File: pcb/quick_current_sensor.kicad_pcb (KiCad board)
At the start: 2 copper layers, 66.2 x 51.8 mm, 23 parts, among them J1 +Vcc, J2 GND, J3 +LOAD, J4 -LOAD, J5 Vout, J6 GND, Q1 MTP2P50E, U1 LM358N, U2 TL431LP

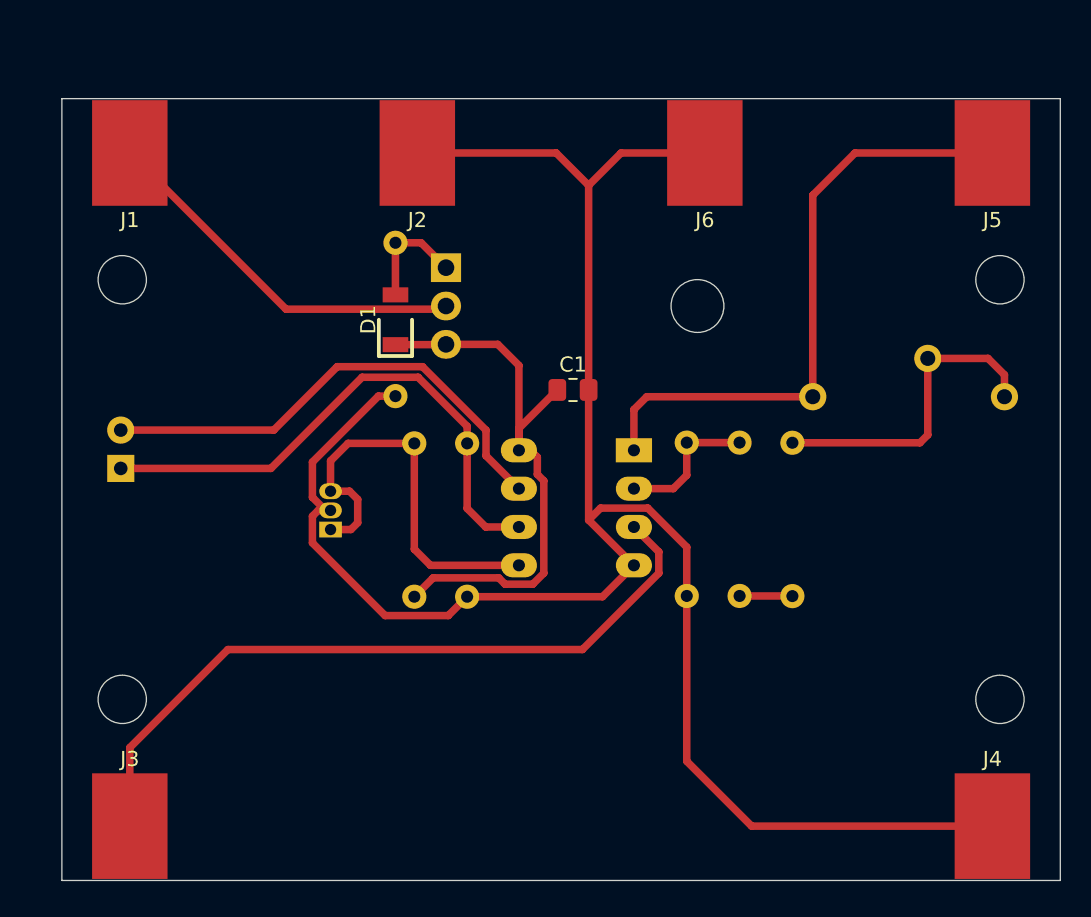
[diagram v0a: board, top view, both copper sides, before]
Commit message: add Rs footprint and 3d model
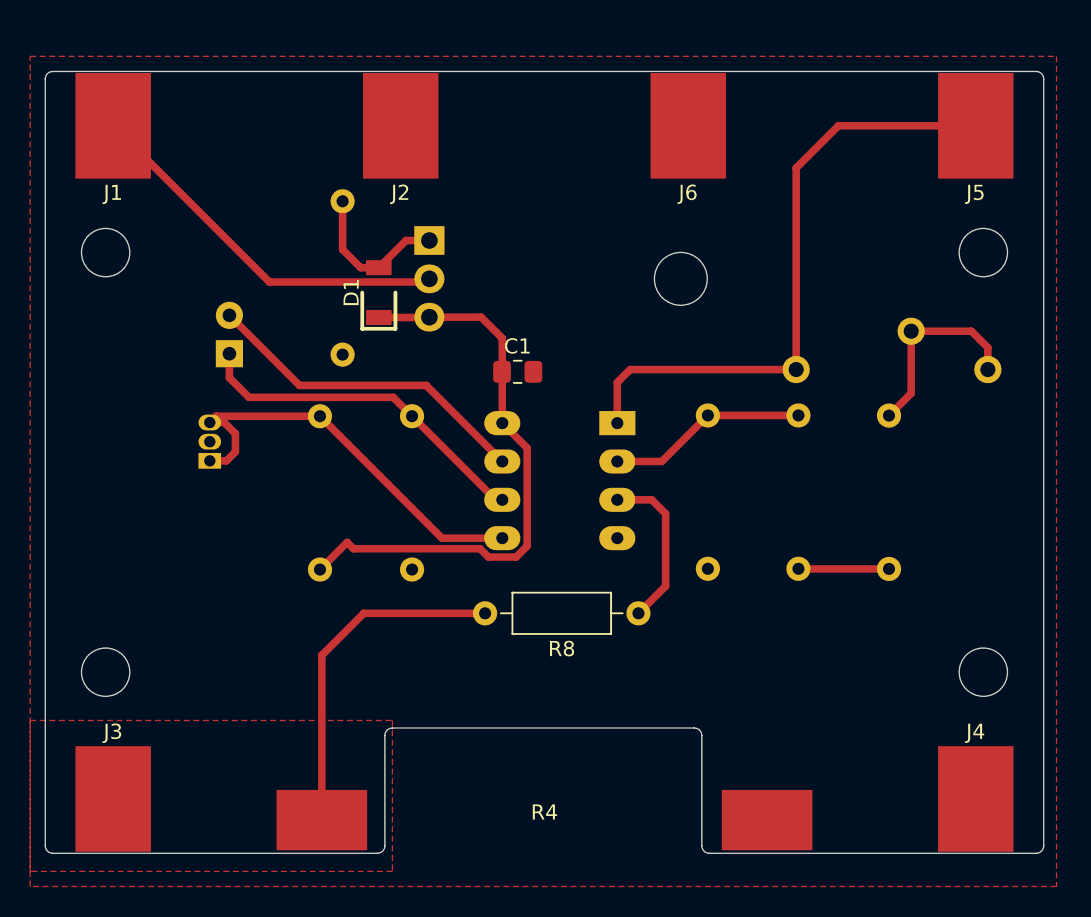
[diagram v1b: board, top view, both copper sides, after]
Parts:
- added R4: Rs, pl_DalePR:RH-10, F.Cu at (113.1, 119.6)
- added R8: 0, Resistor_THT:R_Axial_DIN0207_L6.3mm_D2.5mm_P10.16mm_Horizontal, F.Cu at (119.3, 105.9)
- moved D2 10.5 mm to (92.2, 88.7)
- moved U2 9.20 mm to (90.9, 95.8)
- moved R3 6.65 mm to (135.9, 92.8)
- moved R6 6.50 mm to (98.2, 103.0)
- moved R5 4.45 mm to (99.7, 78.6)
- moved R2 4.30 mm to (129.9, 103.0)
- moved R7 4.07 mm to (104.3, 103.0)
- moved C1 3.85 mm to (111.3, 89.9)
- moved R1 2.28 mm to (123.9, 103.0)
- moved J2 2.11 mm to (103.5, 73.6)
- moved J6 2.11 mm to (122.6, 73.6)
- moved J1 2.11 mm to (84.5, 73.6)
- moved J5 2.11 mm to (141.7, 73.6)
- moved D1 2.11 mm to (102.1, 84.7)
- moved H1 2.11 mm to (84.0, 82.0)
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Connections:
- U1 pad 3: Net-(J3-Pad1) -> Net-(R8-Pad1)
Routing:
- net GND: track 130.4 -> 0.00 mm
- net Net-(J3-Pad1): track 48.8 -> 22.9 mm
- net Net-(D2-Pad1): track 36.2 -> 23.0 mm
- net Net-(R8-Pad1): track 0.00 -> 10.9 mm
- net Net-(D2-Pad2): track 32.5 -> 22.1 mm
- net Net-(R3-Pad1): track 21.2 -> 13.2 mm
- net Net-(R1-Pad2): track 9.53 -> 13.3 mm
- net Net-(D1-Pad2): track 7.48 -> 10.2 mm
- net Net-(R2-Pad1): track 3.50 -> 6.00 mm
- added copper zone on F.Cu, net GND
- added copper zone on F.Cu, net Net-(J3-Pad1)
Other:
- outline, holes or cut-outs redrawn

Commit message: cleanup and add logo
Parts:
- added G***: LOGO, PL_logo:logoInverse_height_10mm, F.Cu at (85.6, 91.1)
- R8: moved to B.Cu
- U2: footprint Package_TO_SOT_THT:TO-92_Inline -> Package_TO_SOT_THT:TO-92_W4.0mm_StaggerEven_Horizontal_FlatSideDown
- moved R6 12.2 mm to (98.1, 90.8), turned to 270 degrees
- moved D2 11.9 mm to (103.1, 93.4), turned to 0 degrees
- moved R2 11.3 mm to (141.2, 103.0), turned to 180 degrees
- moved R1 10.2 mm to (123.9, 92.8), turned to 270 degrees
- moved D1 8.20 mm to (110.3, 84.7)
- moved R3 6.45 mm to (131.0, 97.0), turned to 0 degrees
- moved R7 5.50 mm to (104.4, 108.5)
- moved U2 5.24 mm to (89.7, 100.9), turned to 0 degrees
- moved R5 3.22 mm to (101.6, 81.2), turned to 180 degrees
- moved R8 2.77 mm to (121.1, 108.0)
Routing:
- net VCC: track 38.4 -> 21.1 mm
- net Net-(D2-Pad2): track 22.1 -> 5.65 mm
- net Net-(D2-Pad1): track 23.0 -> 11.4 mm
- net Net-(R3-Pad1): track 13.2 -> 21.2 mm
- net Net-(R6-Pad2): track 28.1 -> 21.2 mm
- net Net-(R1-Pad2): track 13.3 -> 17.8 mm
- net Net-(J5-Pad1): track 41.3 -> 43.9 mm
- net Net-(J3-Pad1): track 22.9 -> 20.5 mm
- net Net-(R8-Pad1): track 10.9 -> 12.2 mm

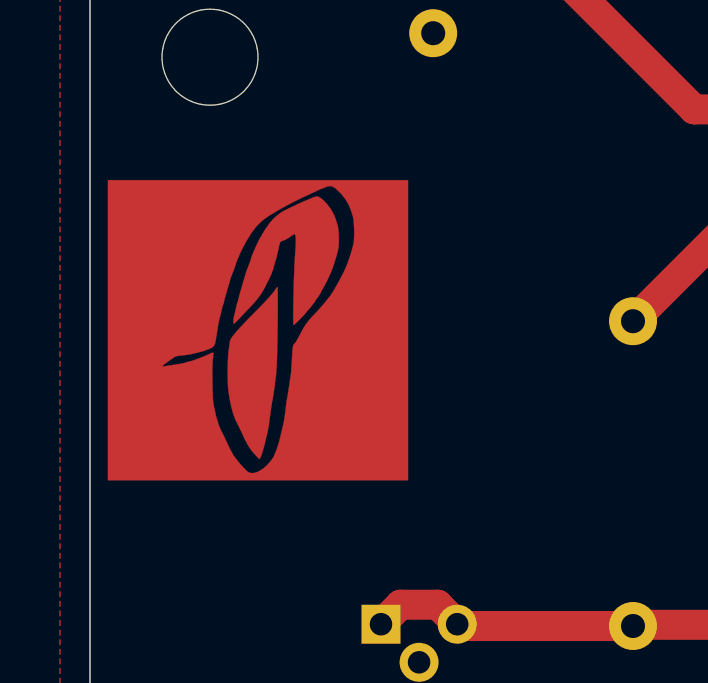
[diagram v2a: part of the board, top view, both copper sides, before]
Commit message: Update quick_current_sensor.kicad_pcb
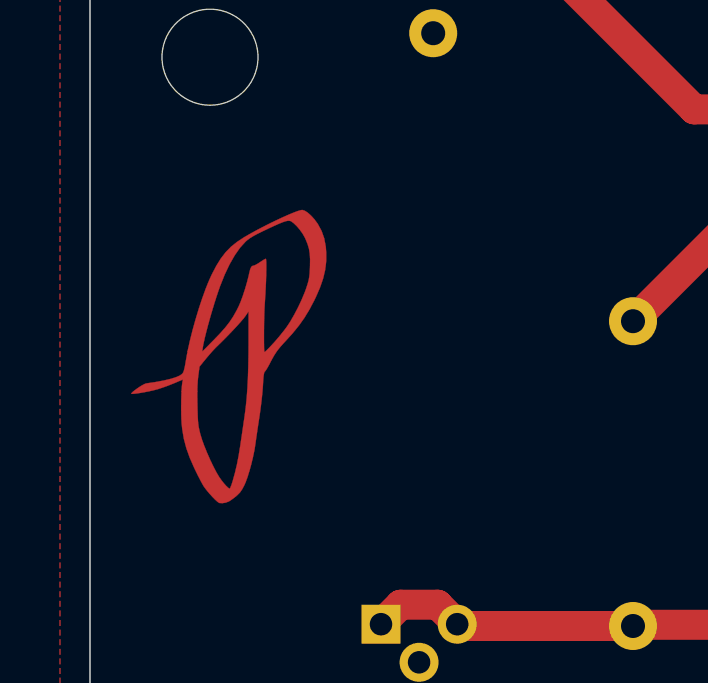
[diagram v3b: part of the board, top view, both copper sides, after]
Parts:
- removed the G*** at (85.6, 91.1)
- added G***: LOGO, PL_logo:logo_height_10mm, F.Cu at (84.6, 92.0)

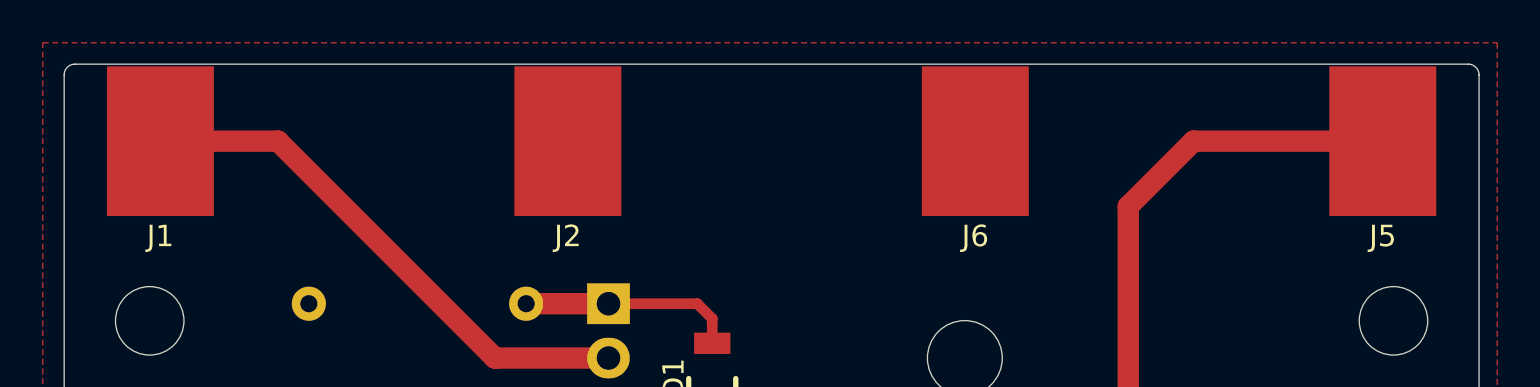
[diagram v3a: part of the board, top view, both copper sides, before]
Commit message: change power and vout to terminal blocks
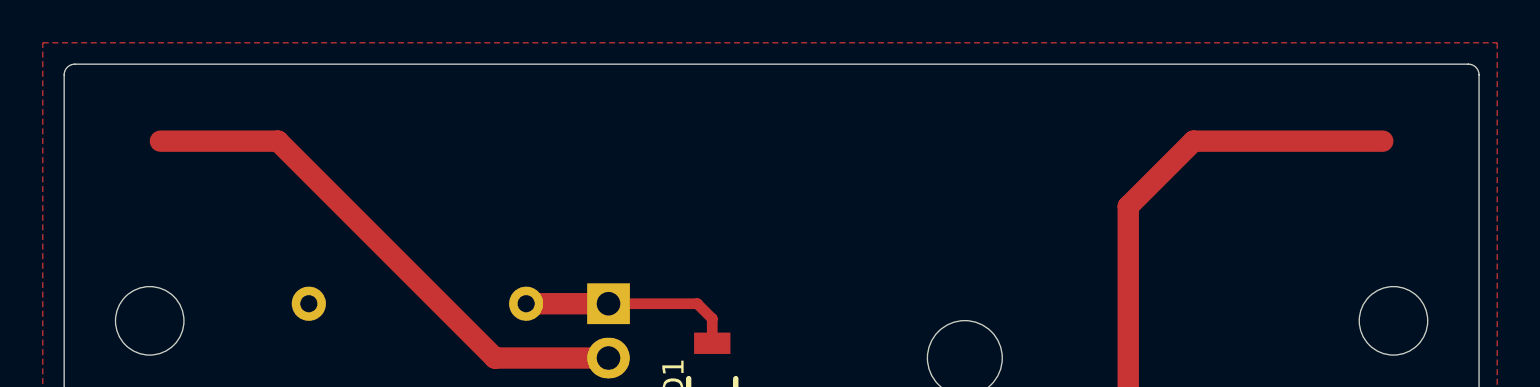
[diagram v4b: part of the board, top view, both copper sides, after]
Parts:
- removed J1: +Vcc, pl_Banana:banana_edge_mount
- removed J2, J6: GND, pl_Banana:banana_edge_mount
- removed J5: Vout, pl_Banana:banana_edge_mount

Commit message: cleanup, reduce size
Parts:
- removed H1, H2, H3, H4: MountingHole, MountingHole:MountingHole_3.2mm_M3
- removed R8: 0, Resistor_THT:R_Axial_DIN0207_L6.3mm_D2.5mm_P10.16mm_Horizontal
- added J1: PWR, pl_TerminalBlock:WJ127-5.0-2P, B.Cu at (95.0, 74.0)
- added J2: OUT, pl_TerminalBlock:WJ127-5.0-2P, B.Cu at (131.0, 74.0)
- added REF**: MountingHole_3.2mm_M3, MountingHole:MountingHole_3.2mm_M3, F.Cu at (138.5, 72.5)
- added REF**: MountingHole_3.2mm_M3, MountingHole:MountingHole_3.2mm_M3, F.Cu at (87.0, 72.5)
- J4: value -LOAD -> GND
- moved RV1 9.50 mm to (122.0, 95.2)
- moved R2 8.14 mm to (135.2, 108.5)
- moved R3 8.14 mm to (125.0, 102.5)
- moved G*** 7.57 mm to (91.8, 89.5)
- moved J4 6.65 mm to (135.0, 118.0)
- moved J3 6.50 mm to (91.0, 118.0)
- moved R1 5.85 mm to (121.9, 98.3)
- moved C1 2.00 mm to (109.3, 89.9)
- moved D1 2.00 mm to (108.3, 84.7)
- moved D2 2.00 mm to (101.1, 93.4)
- moved Q1 2.00 mm to (103.5, 81.2)
- moved R5 2.00 mm to (99.6, 81.2)
- moved R6 2.00 mm to (96.1, 90.8)
- moved R7 2.00 mm to (102.4, 108.5)
- moved U1 2.00 mm to (115.9, 93.3)
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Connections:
- U1 pad 3: Net-(R8-Pad1) -> Net-(J3-Pad1)
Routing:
- net Net-(J3-Pad1): track 20.5 -> 38.7 mm
- net Net-(R8-Pad1): track 12.2 -> 0.00 mm
- net Net-(J2-Pad1): track 43.9 -> 31.9 mm
- net Net-(J1-Pad1): track 25.2 -> 16.7 mm
- net Net-(R3-Pad1): track 21.2 -> 17.8 mm
- net Net-(R1-Pad2): track 17.8 -> 19.5 mm
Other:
- board size 66.2 x 51.8 mm -> 56.5 x 51.5 mm
